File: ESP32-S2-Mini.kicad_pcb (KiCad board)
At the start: 2 copper layers, 27.9 x 55.9 mm, 14 parts, among them J1 Conn_01x21, J2 Conn_01x21, J3 Conn_02x03_Odd_Even, J4 Conn_02x05_Odd_Even, U1 TC2117-3.3VDBTR, U2 ESP32-S2-MINI-1

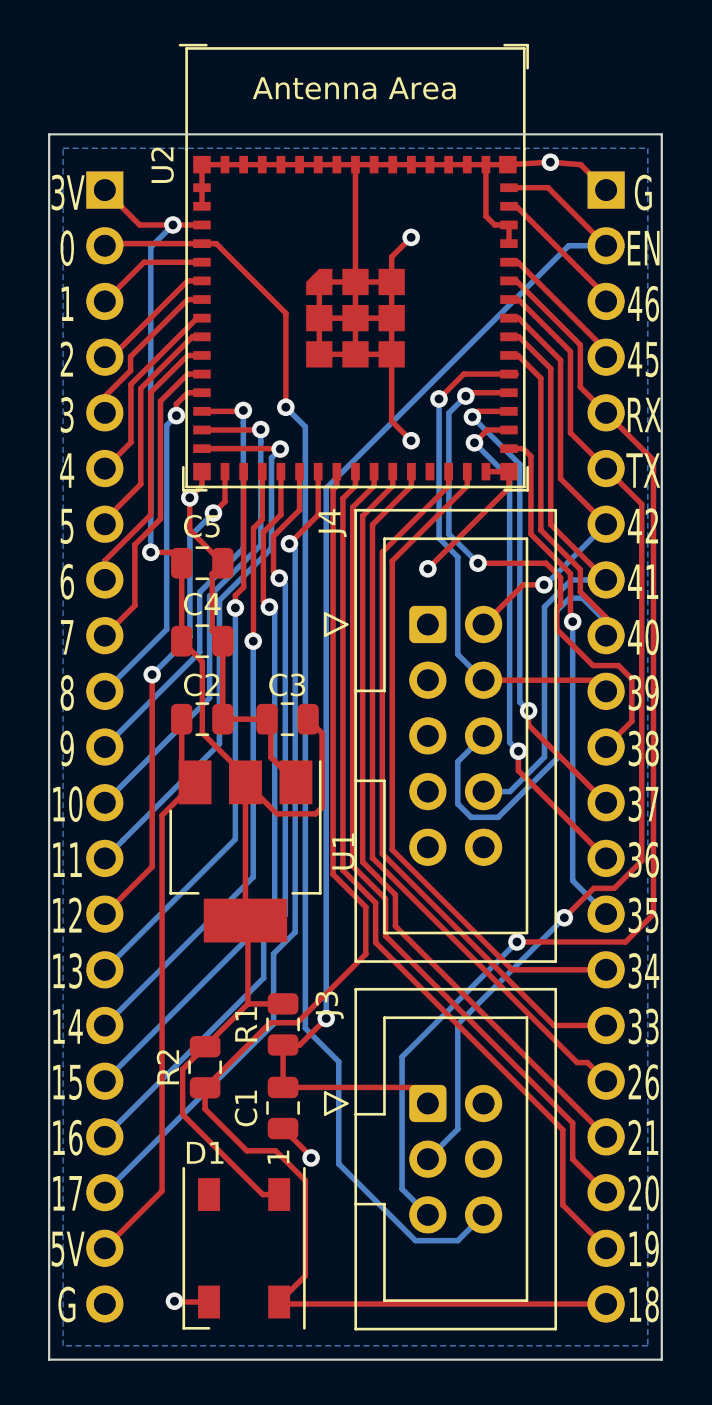
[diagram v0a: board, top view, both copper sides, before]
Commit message: Reroute rx/tx inside the board
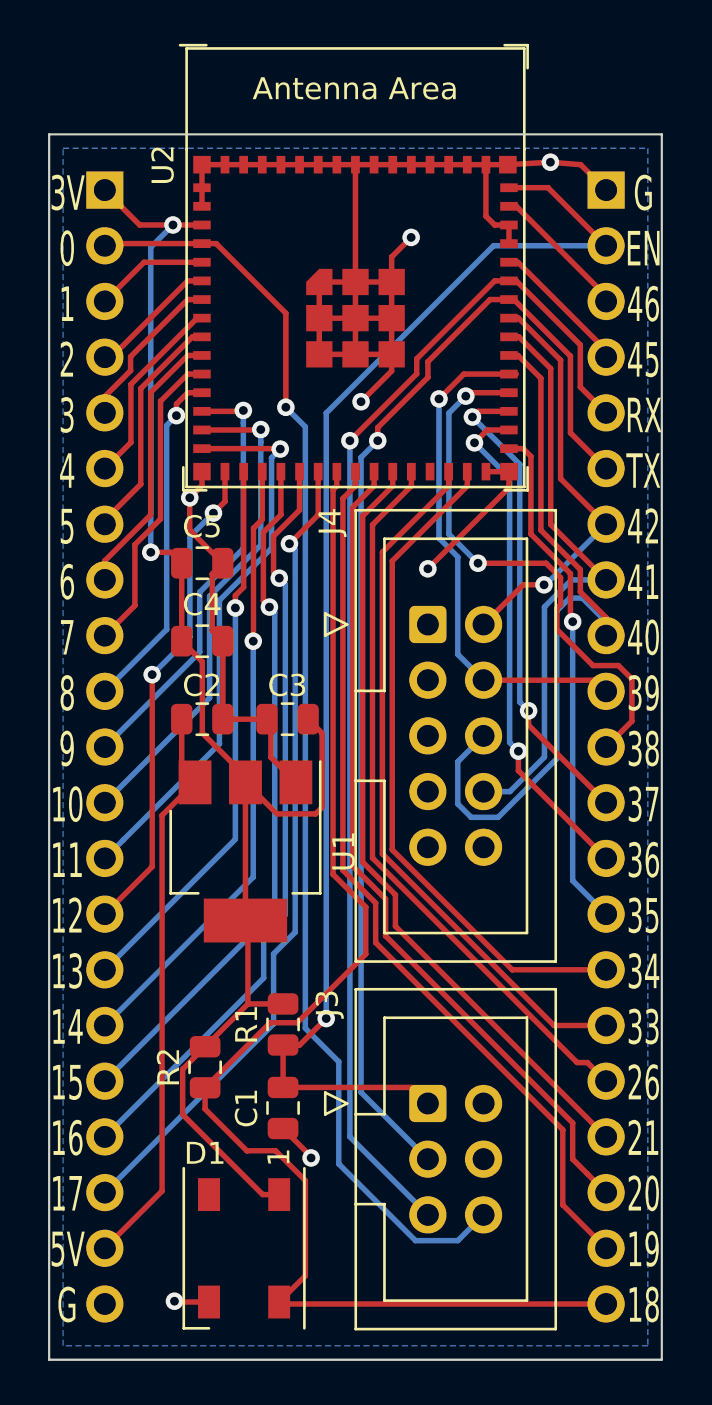
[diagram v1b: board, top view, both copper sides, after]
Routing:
- net /TX: track 46.6 -> 53.4 mm
- net /RESET: track 58.4 -> 60.4 mm
- net /RX: track 53.7 -> 55.5 mm
- net GND: track 86.4 -> 84.8 mm
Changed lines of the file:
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@@
     (thickness 1.6)
     (drawings 6)
-    (tracks 396)
+    (tracks 395)
     (zones 0)
     (modules 14)
@@
   (segment (start 196.85 110.109) (end 198.0565 108.9025) (width 0.25) (layer F.Cu) (net 1))
   (segment (start 196.088 110.109) (end 196.85 110.109) (width 0.25) (layer F.Cu) (net 1))
-  (segment (start 210.82 73.66) (end 209.111998 73.66) (width 0.25) (layer B.Cu) (net 1))
-  (segment (start 198.0565 84.715498) (end 198.0565 108.9025) (width 0.25) (layer B.Cu) (net 1))
-  (segment (start 209.111998 73.66) (end 198.0565 84.715498) (width 0.25) (layer B.Cu) (net 1))
+  (segment (start 210.82 73.66) (end 205.682998 73.66) (width 0.25) (layer B.Cu) (net 1))
+  (segment (start 205.682998 73.66) (end 198.0565 81.286498) (width 0.25) (layer B.Cu) (net 1))
+  (segment (start 198.0565 81.286498) (end 198.0565 108.9025) (width 0.25) (layer B.Cu) (net 1))
   (segment (start 193.3425 91.694) (end 193.3425 95.25) (width 0.25) (layer F.Cu) (net 2))
   (segment (start 193.3425 95.25) (end 193.421 95.25) (width 0.25) (layer F.Cu) (net 2))
@@
   (segment (start 195.5315 96.9905) (end 196.6735 98.1325) (width 0.25) (layer F.Cu) (net 2))
   (segment (start 195.5315 95.25) (end 195.5315 96.9905) (width 0.25) (layer F.Cu) (net 2))
-  (via (at 201.93 82.55) (size 0.8) (drill 0.4) (layers F.Cu B.Cu) (net 2))
-  (segment (start 201.04 78.612) (end 201.04 81.66) (width 0.25) (layer F.Cu) (net 2))
-  (segment (start 201.04 81.66) (end 201.93 82.55) (width 0.25) (layer F.Cu) (net 2))
   (via (at 191.8335 85.1535) (size 0.8) (drill 0.4) (layers F.Cu B.Cu) (net 2))
   (segment (start 193.3425 88.138) (end 191.8335 86.629) (width 0.25) (layer F.Cu) (net 2))
@@
   (segment (start 206.39 83.962) (end 206.39 84.694012) (width 0.25) (layer F.Cu) (net 2))
   (segment (start 206.39 84.694012) (end 202.692012 88.392) (width 0.25) (layer F.Cu) (net 2))
+  (segment (start 201.04 78.612) (end 201.04 79.376) (width 0.25) (layer F.Cu) (net 2))
+  (via (at 199.644 80.772) (size 0.8) (drill 0.4) (layers F.Cu B.Cu) (net 2))
+  (segment (start 201.04 79.376) (end 199.644 80.772) (width 0.25) (layer F.Cu) (net 2))
   (segment (start 190.569009 99.636991) (end 192.0735 98.1325) (width 0.25) (layer F.Cu) (net 3))
   (segment (start 190.569009 116.770991) (end 190.569009 99.636991) (width 0.25) (layer F.Cu) (net 3))
@@
   (segment (start 206.827625 76.962) (end 208.744979 78.879354) (width 0.25) (layer F.Cu) (net 37))
   (segment (start 206.39 76.962) (end 206.827625 76.962) (width 0.25) (layer F.Cu) (net 37))
-  (via (at 208.915 104.305994) (size 0.8) (drill 0.4) (layers F.Cu B.Cu) (net 38))
-  (segment (start 202.692 115.316) (end 204.056999 113.951001) (width 0.25) (layer B.Cu) (net 38))
-  (segment (start 212.44501 101.713992) (end 211.194003 102.964999) (width 0.25) (layer F.Cu) (net 38))
-  (segment (start 211.194003 102.964999) (end 210.255995 102.964999) (width 0.25) (layer F.Cu) (net 38))
-  (segment (start 204.056999 113.951001) (end 204.056999 109.163995) (width 0.25) (layer B.Cu) (net 38))
-  (segment (start 204.056999 109.163995) (end 208.915 104.305994) (width 0.25) (layer B.Cu) (net 38))
-  (segment (start 210.82 83.82) (end 212.44501 85.44501) (width 0.25) (layer F.Cu) (net 38))
-  (segment (start 212.44501 85.44501) (end 212.44501 101.713992) (width 0.25) (layer F.Cu) (net 38))
-  (segment (start 210.255995 102.964999) (end 208.915 104.305994) (width 0.25) (layer F.Cu) (net 38))
-  (segment (start 209.194989 82.194989) (end 210.82 83.82) (width 0.25) (layer F.Cu) (net 38))
-  (segment (start 209.194989 78.483488) (end 209.194989 82.194989) (width 0.25) (layer F.Cu) (net 38))
-  (segment (start 206.823501 76.112) (end 209.194989 78.483488) (width 0.25) (layer F.Cu) (net 38))
-  (segment (start 206.39 76.112) (end 206.823501 76.112) (width 0.25) (layer F.Cu) (net 38))
-  (segment (start 212.979 104.14) (end 211.709 105.41) (width 0.25) (layer F.Cu) (net 39))
-  (segment (start 211.709 105.41) (end 206.756 105.41) (width 0.25) (layer F.Cu) (net 39))
-  (segment (start 210.82 81.28) (end 212.979 83.439) (width 0.25) (layer F.Cu) (net 39))
-  (segment (start 201.516999 116.680999) (end 202.692 117.856) (width 0.25) (layer B.Cu) (net 39))
-  (segment (start 212.979 83.439) (end 212.979 104.14) (width 0.25) (layer F.Cu) (net 39))
-  (segment (start 209.644999 78.181997) (end 209.644999 80.104999) (width 0.25) (layer F.Cu) (net 39))
+  (segment (start 209.19499 82.19499) (end 210.82 83.82) (width 0.25) (layer F.Cu) (net 38))
+  (segment (start 209.19499 78.692955) (end 209.19499 82.19499) (width 0.25) (layer F.Cu) (net 38))
+  (segment (start 206.614035 76.112) (end 209.19499 78.692955) (width 0.25) (layer F.Cu) (net 38))
+  (segment (start 206.39 76.112) (end 206.614035 76.112) (width 0.25) (layer F.Cu) (net 38))
+  (via (at 200.406 82.55) (size 0.8) (drill 0.4) (layers F.Cu B.Cu) (net 38))
+  (segment (start 199.644 112.268) (end 202.692 115.316) (width 0.25) (layer B.Cu) (net 38))
+  (segment (start 199.644 83.312) (end 199.644 112.268) (width 0.25) (layer B.Cu) (net 38))
+  (segment (start 200.406 82.55) (end 199.644 83.312) (width 0.25) (layer B.Cu) (net 38))
+  (segment (start 202.692 79.663999) (end 200.406 81.949999) (width 0.25) (layer F.Cu) (net 38))
+  (segment (start 200.406 81.949999) (end 200.406 82.55) (width 0.25) (layer F.Cu) (net 38))
+  (segment (start 202.692 78.95) (end 202.692 79.663999) (width 0.25) (layer F.Cu) (net 38))
+  (segment (start 205.53 76.112) (end 202.692 78.95) (width 0.25) (layer F.Cu) (net 38))
+  (segment (start 206.39 76.112) (end 205.53 76.112) (width 0.25) (layer F.Cu) (net 38))
   (segment (start 209.644999 80.104999) (end 210.82 81.28) (width 0.25) (layer F.Cu) (net 39))
   (segment (start 206.725002 75.262) (end 209.644999 78.181997) (width 0.25) (layer F.Cu) (net 39))
+  (segment (start 209.644999 78.181997) (end 209.644999 80.104999) (width 0.25) (layer F.Cu) (net 39))
   (segment (start 206.39 75.262) (end 206.725002 75.262) (width 0.25) (layer F.Cu) (net 39))
-  (segment (start 206.756 105.41) (end 201.516999 110.649001) (width 0.25) (layer B.Cu) (net 39))
-  (segment (start 201.516999 110.649001) (end 201.516999 116.680999) (width 0.25) (layer B.Cu) (net 39))
-  (via (at 206.756 105.41) (size 0.8) (drill 0.4) (layers F.Cu B.Cu) (net 39))
+  (via (at 199.136 82.55) (size 0.8) (drill 0.4) (layers F.Cu B.Cu) (net 39))
+  (segment (start 199.136 114.3) (end 202.692 117.856) (width 0.25) (layer B.Cu) (net 39))
+  (segment (start 199.136 82.55) (end 199.136 114.3) (width 0.25) (layer B.Cu) (net 39))
+  (segment (start 202.184 79.502) (end 199.136 82.55) (width 0.25) (layer F.Cu) (net 39))
+  (segment (start 202.184 78.818) (end 202.184 79.502) (width 0.25) (layer F.Cu) (net 39))
+  (segment (start 205.74 75.262) (end 202.184 78.818) (width 0.25) (layer F.Cu) (net 39))
+  (segment (start 206.39 75.262) (end 205.74 75.262) (width 0.25) (layer F.Cu) (net 39))
   (segment (start 210.82 78.432999) (end 210.82 78.74) (width 0.25) (layer F.Cu) (net 40))
   (segment (start 206.799001 74.412) (end 210.82 78.432999) (width 0.25) (layer F.Cu) (net 40))

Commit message: Shrink the board slightly to fit better on a breadboard
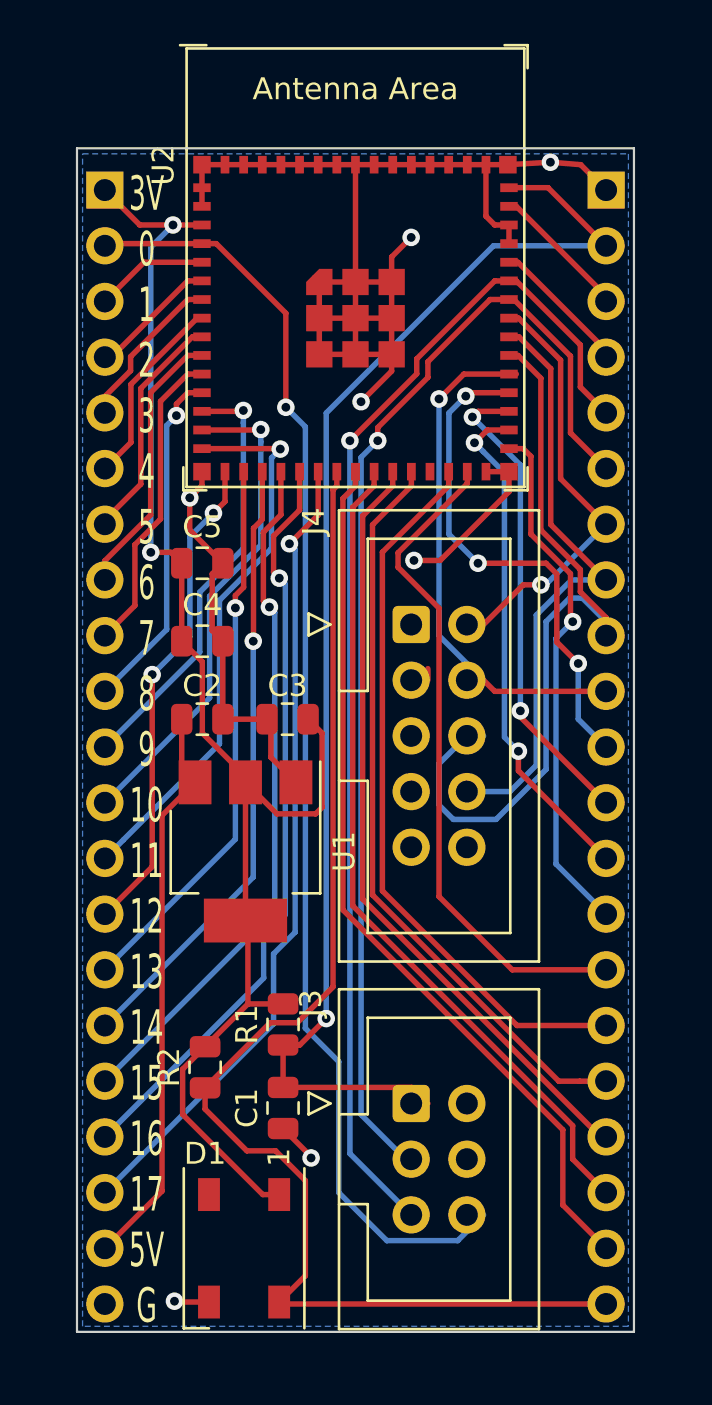
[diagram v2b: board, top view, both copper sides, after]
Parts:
- moved J3 0.76 mm to (201.9, 112.8)
- moved J4 0.76 mm to (201.9, 90.9)
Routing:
- net /GPIO38: track 24.9 -> 23.1 mm, vias 2 -> 3
- net /GPIO40: track 34.6 -> 36.4 mm
- net /GPIO18: track 60.4 -> 59.2 mm
- net /GPIO33: track 32.1 -> 33.1 mm
- net /GPIO26: track 33.2 -> 34.2 mm
- net /GPIO0: track 57.9 -> 58.7 mm
- net /GPIO35: track 23.4 -> 24.1 mm
- net GND: track 84.8 -> 85.4 mm
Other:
- board size 27.9 x 55.9 mm -> 25.4 x 54 mm
- board text removed: "G EN 46 45 RX TX 42 41 40 39 38 37 36 35 34 33 26 21 20 19 18"
